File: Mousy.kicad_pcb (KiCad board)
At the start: 2 copper layers, 31.2 x 36.3 mm, 4 parts, among them J1 Mouse_out, J2 Mouse_in, U1 74LS125

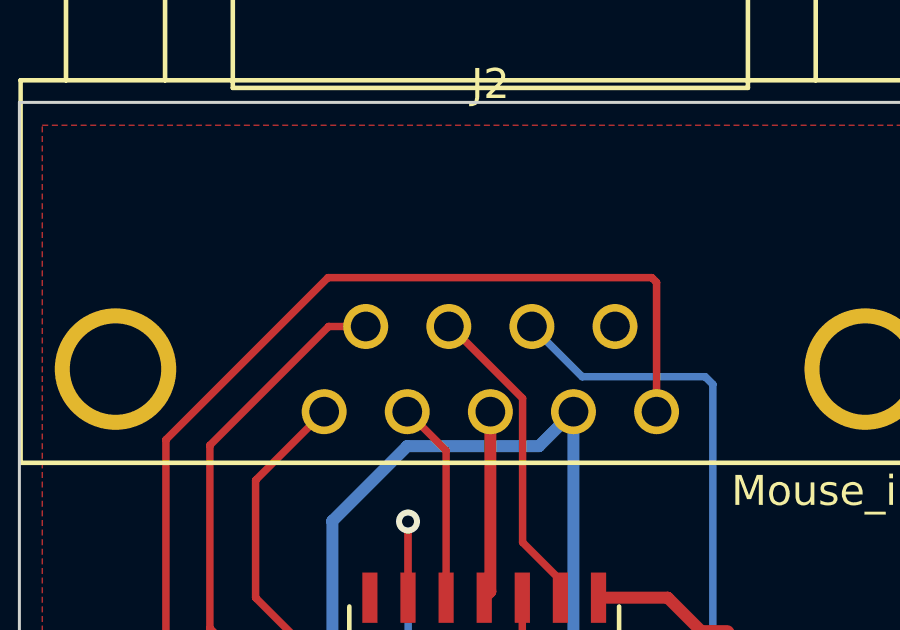
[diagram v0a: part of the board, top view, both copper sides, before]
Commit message: add mouse, fix some gnd nets
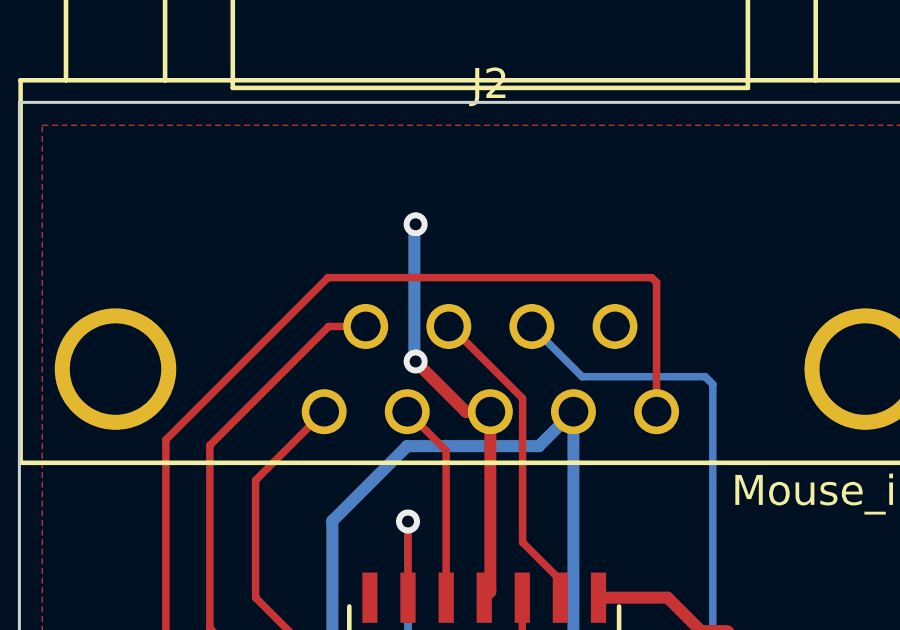
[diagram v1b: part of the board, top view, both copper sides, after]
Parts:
- added Logo1: Mouse-, localfootprints:Mouse+, B.Cu at (191.3, 70.9)
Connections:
- U1 pad 14: VCC -> (no net)
- U1 pad 7: GND -> (no net)
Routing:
- net GND: track 21.0 -> 28.8 mm, vias 2 -> 4
